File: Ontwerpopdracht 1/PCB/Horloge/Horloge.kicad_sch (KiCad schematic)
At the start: 28 parts

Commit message: update schema
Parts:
- removed S?: EVQ-P7L01P, SW_EVQ-P7L01P, symbol EVQ-P7L01P:EVQ-P7L01P
- removed Y?: FX135A-327, OSCCC150X320X90-2N, symbol FX135A-327:FX135A-327
- added U?: ATtiny412-SS, Package_SO:SOIC-8_3.9x4.9mm_P1.27mm, symbol MCU_Microchip_ATtiny:ATtiny412-SS
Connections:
- net +5V: now also S?.1_1, S?.1_1, S?.1_1, S?.1_2, S?.1_2, S?.1_2, U?.1 (VCC)
- net GND: now also U?.8 (GND)
- net +3V0: now reaches U?.3 (VIN)
- net LEDs uren: now reaches D?.4 (DIN)
- net LEDs uren: now also U?.5 (PA2)
- net Knop rechts: now reaches S?.2_1, S?.2_2
- net Knop rechts: now also U?.2 (PA6)
- net Knop midden: now reaches S?.2_1, S?.2_2
- net Knop midden: now also U?.3 (PA7)
- net Knop links: now reaches S?.2_1, S?.2_2
- net Knop links: now also U?.4 (PA1)
- net LEDs minuten: now reaches D?.4 (DIN)
- net LEDs minuten: now also U?.7 (PA3)
- new net Programming header: U?.6 (~{RESET}/PA0)
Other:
- moved on the sheet: S?, U?

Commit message: schema
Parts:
- removed D? (x20): WS2812B, LED_SMD:LED_WS2812B_PLCC4_5.0x5.0mm_P3.2mm, symbol LED:WS2812B
- removed U?: LDL1117S50R_, SOT230P700X180-4N, symbol LDL1117S50R_:LDL1117S50R_
- removed U?: ATtiny412-SS, Package_SO:SOIC-8_3.9x4.9mm_P1.27mm, symbol MCU_Microchip_ATtiny:ATtiny412-SS
- added BT1: Battery_Cell, symbol Device:Battery_Cell
- added D10, D11, D12, D13, D14, D15, D16, D17, D18, D19, D20, D21, D22, D23, D24, D3, D4, D5, D6, D7, D8, D9: WS2812B, LED_SMD:LED_WS2812B-2020_PLCC4_2.0x2.0mm, symbol LED:WS2812B
- added J1: Conn_01x03, symbol Connector_Generic:Conn_01x03
- added J1, J2: Conn_01x01, symbol Connector_Generic:Conn_01x01
- added Q1: BSS138, Package_TO_SOT_SMD:SOT-23, symbol Transistor_FET:BSS138
- added U1: TPS613222ADBVT, TPS613222ADBVT:SOT95P280X145-5N, symbol TPS613222ADBVT:TPS613222ADBVT
- added U1: ATTINY1614-SSF, ATTINY1614-SSF:SOIC127P600X175-14N, symbol ATTINY1614-SSF:ATTINY1614-SSF
- added Y1: FX135A-327, FX135A-327:OSCCC150X320X90-2N, symbol FX135A-327:FX135A-327
- D1, D2: renamed from D?; footprint LED_SMD:LED_WS2812B_PLCC4_5.0x5.0mm_P3.2mm -> LED_SMD:LED_WS2812B-2020_PLCC4_2.0x2.0mm
- S1, S2, S3: renamed from S?; footprint SW_EVQ-P7L01P -> EVQ-P7L01P:SW_EVQ-P7L01P
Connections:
- net +5V: now also J1.1 (Pin_1), Q1.2 (S), U1.1 (VDD), U1.4 (VOUT); no longer D1.3 (VSS), D2.3 (VSS)
- net GND: now also BT1.2 (-), D10.1 (VDD), D11.1 (VDD), D12.1 (VDD), D13.1 (VDD), D14.1 (VDD), D15.1 (VDD), D16.1 (VDD), D17.1 (VDD), D18.1 (VDD), D19.1 (VDD), D20.1 (VDD), D21.1 (VDD), D22.1 (VDD), D23.1 (VDD), D24.1 (VDD), D3.1 (VDD), D4.1 (VDD), D5.1 (VDD), D6.1 (VDD), D7.1 (VDD), D8.1 (VDD), D9.1 (VDD), J1.3 (Pin_3), U1.14 (GND), U1.2 (GND)
- net Knop links: now also U1.9 (PB0)
- net Knop midden: now also U1.5 (PA7)
- net Knop rechts: now also U1.4 (PA6)
- net LEDs minuten: now also D13.4 (DIN), J2.1 (Pin_1), U1.11 (PA1)
- net LEDs uren: now also J1.1 (Pin_1), U1.12 (PA2)
- net at D2.2 (DOUT): now also D3.4 (DIN)
- new net: D15.2 (DOUT), D16.4 (DIN)
- new net: D14.2 (DOUT), D15.4 (DIN)
- new net: D13.2 (DOUT), D14.4 (DIN)
- new net: D22.2 (DOUT), D23.4 (DIN)
- new net: D21.2 (DOUT), D22.4 (DIN)
- new net: D6.2 (DOUT), D7.4 (DIN)
- new net: D5.2 (DOUT), D6.4 (DIN)
- new net: D8.2 (DOUT), D9.4 (DIN)
- new net: D7.2 (DOUT), D8.4 (DIN)
- new net: D17.2 (DOUT), D18.4 (DIN)
- new net: D16.2 (DOUT), D17.4 (DIN)
- new net: D23.2 (DOUT), D24.4 (DIN)
- new net: D11.2 (DOUT), D12.4 (DIN)
- new net: D10.2 (DOUT), D11.4 (DIN)
- new net: D10.4 (DIN), D9.2 (DOUT)
- new net: D4.2 (DOUT), D5.4 (DIN)
- new net: D20.2 (DOUT), D21.4 (DIN)
- new net: D19.2 (DOUT), D20.4 (DIN)
- new net: D3.2 (DOUT), D4.4 (DIN)
- new net: D18.2 (DOUT), D19.4 (DIN)
- new net LEDs uit: Q1.1 (G), U1.8 (PB1)
- new net TOSC1: U1.6 (PB3/OSC1), Y1.1
- new net TOSC2: U1.7 (PB2/OSC2), Y1.2
- new net UDPI: J1.2 (Pin_2), U1.10 (PA0/~{RESET~{/UDPI})
- new net VCC: BT1.1 (+), U1.1 (SW)
- new net VSS: D1.3 (VSS), D10.3 (VSS), D11.3 (VSS), D12.3 (VSS), D13.3 (VSS), D14.3 (VSS), D15.3 (VSS), D16.3 (VSS), D17.3 (VSS), D18.3 (VSS), D19.3 (VSS), D2.3 (VSS), D20.3 (VSS), D21.3 (VSS), D22.3 (VSS), D23.3 (VSS), D24.3 (VSS), D3.3 (VSS), D4.3 (VSS), D5.3 (VSS), D6.3 (VSS), D7.3 (VSS), D8.3 (VSS), D9.3 (VSS), Q1.3 (D)
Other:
- note added: "ATTINY1614-SSF"
- note added: "BATTERIJ"
- note added: "KNOPPEN"
- note added: "KRISTAL"
- note added: "LED SWITCH"
- note added: "LEDS MINUTEN"
- note added: "LEDS UREN"
- note added: "PROGRAMMEERPIN"
- note added: "SPANNINGSREGELAAR"
- moved on the sheet: D1, D2, S1, S2, S3

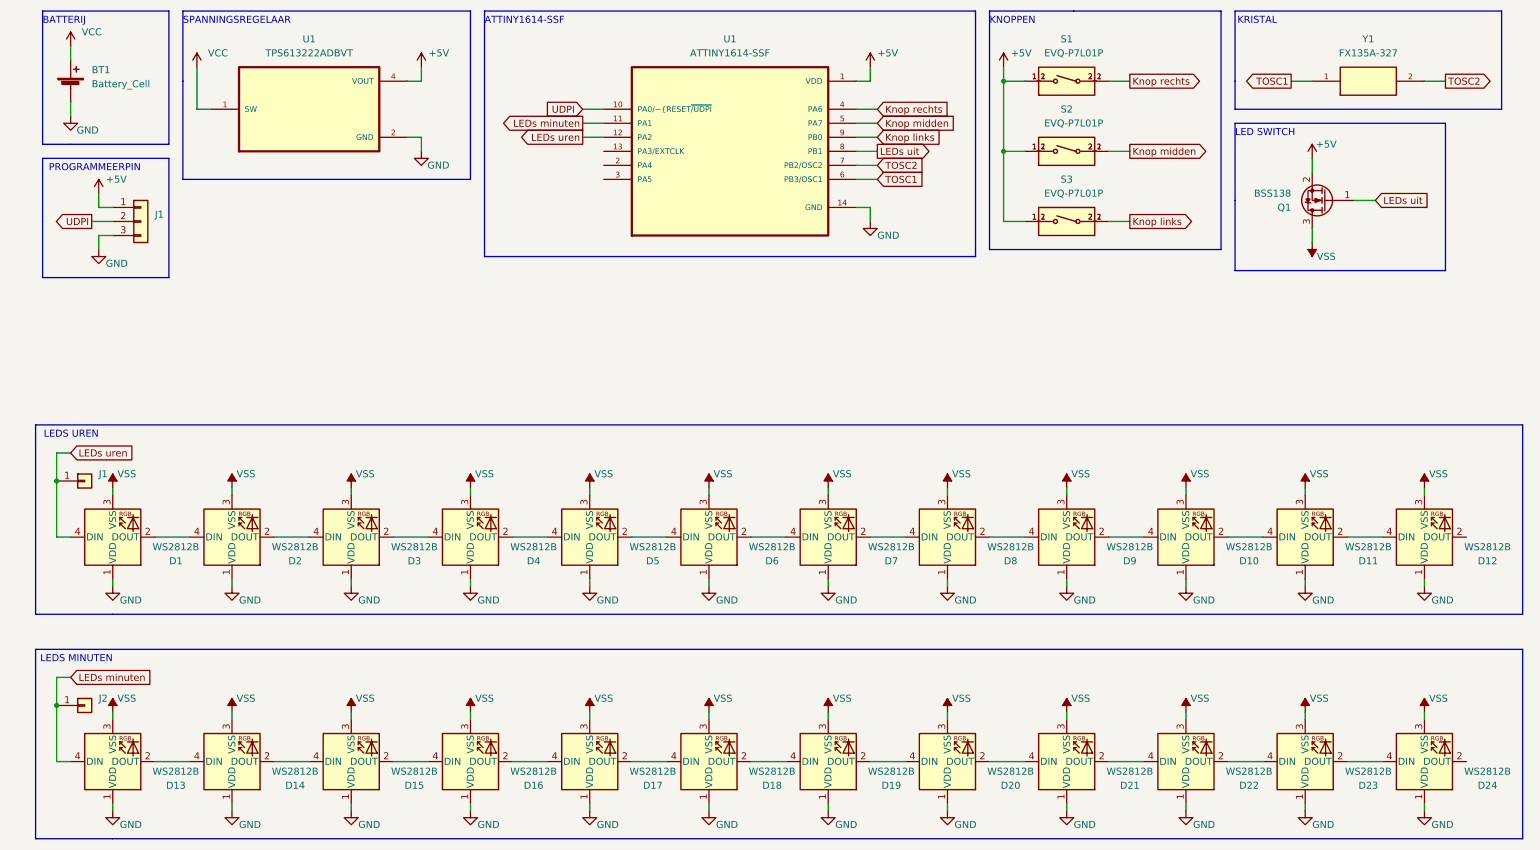
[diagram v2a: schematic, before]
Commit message: update schema + doc scema
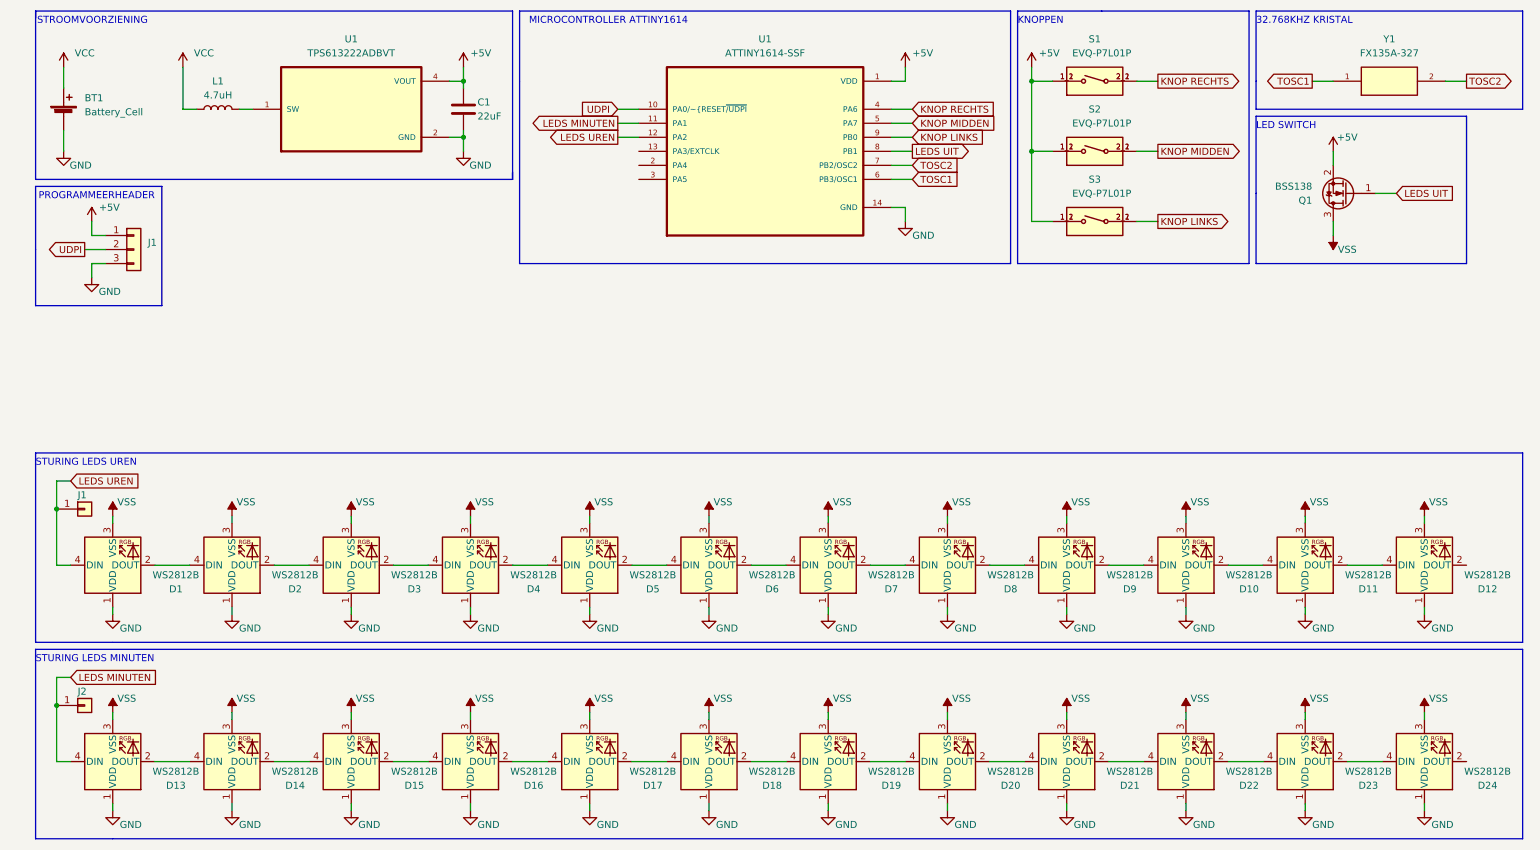
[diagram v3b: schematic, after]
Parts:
- added C1: 22uF, symbol Device:C
- added L1: 4.7uH, symbol Device:L
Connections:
- net +5V: now also C1.1
- net GND: now also C1.2
- net VCC: now also L1.1; no longer U1.1 (SW)
- net Knop links renamed KNOP LINKS
- net Knop midden renamed KNOP MIDDEN
- net Knop rechts renamed KNOP RECHTS
- net LEDs minuten renamed LEDS MINUTEN
- net LEDs uit renamed LEDS UIT
- net LEDs uren renamed LEDS UREN
- new net: L1.2, U1.1 (SW)
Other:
- note added: "32.768KHZ KRISTAL"
- note added: "MICROCONTROLLER ATTINY1614"
- note added: "PROGRAMMEERHEADER"
- note added: "STROOMVOORZIENING"
- note added: "STURING LEDS MINUTEN"
- note added: "STURING LEDS UREN"
- note removed: "ATTINY1614-SSF"
- note removed: "BATTERIJ"
- note removed: "KRISTAL"
- note removed: "LEDS MINUTEN"
- note removed: "LEDS UREN"
- note removed: "PROGRAMMEERPIN"
- note removed: "SPANNINGSREGELAAR"
- moved on the sheet: BT1, D1, D10, D11, D12, D2, D3, D4, D5, D6, D7, D8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

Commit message: aanpassing attiny, update doc schema
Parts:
- removed U1: ATTINY1614-SSF, ATTINY1614-SSF:SOIC127P600X175-14N, symbol ATTINY1614-SSF:ATTINY1614-SSF
- added U1: ATTINY414-SSF, SOIC127P600X175-14N, symbol ATTINY414-SSF:ATTINY414-SSF
- C1: footprint (none) -> GRM21BR61A226ME51L:CAPC2012X140N
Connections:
- net +5V: now also U1.1 (VDD)
- net GND: now also U1.14 (GND)
- net KNOP LINKS: now also U1.8 (PB1)
- net KNOP MIDDEN: now also U1.5 (PA7)
- net KNOP RECHTS: now also U1.4 (PA6)
- net LEDS MINUTEN: now also U1.11 (PA1)
- net LEDS UIT: now also U1.9 (PB0)
- net LEDS UREN: now also U1.12 (PA2)
- net TOSC1: now also U1.6 (TOSC1/PB3)
- net TOSC2: now also U1.7 (TOSC2/PB2)
- net UDPI: now also U1.10 (PA0/~{RESET~{/UPDI})
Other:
- note added: "MICROCONTROLLER ATTINY414"
- note removed: "MICROCONTROLLER ATTINY1614"

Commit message: aanpassing schema
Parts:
- added C2, C3: 12pF, GRM21BR61A226ME51L:CAPC2012X140N, symbol Device:C
- added R1, R2, R3: 4k7, symbol Device:R
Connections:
- net +5V: now also R1.1, R2.1, R3.1; no longer S1.1_1, S1.1_2, S2.1_1, S2.1_2, S3.1_1, S3.1_2
- net GND: now also S1.1_1, S1.1_2, S2.1_1, S2.1_2, S3.1_1, S3.1_2, C2.2, C3.2
- net KNOP LINKS: now also R3.2
- net KNOP MIDDEN: now also R2.2
- net KNOP RECHTS: now also R1.2
- net TOSC1: now also C2.1
- net TOSC2: now also C3.1
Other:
- moved on the sheet: Q1, S1, S2, S3, Y1

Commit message: update schema
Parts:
- J1: footprint (none) -> Connector_PinHeader_1.00mm:PinHeader_1x03_P1.00mm_Vertical
- J2: renamed from J1; footprint (none) -> Connector_PinHeader_2.00mm:PinHeader_1x01_P2.00mm_Vertical
- J3: renamed from J2; footprint (none) -> Connector_PinHeader_2.00mm:PinHeader_1x01_P2.00mm_Vertical
- R1, R2, R3: footprint (none) -> Resistor_SMD:R_0805_2012Metric_Pad1.20x1.40mm_HandSolder
- renumbered U1 to U2
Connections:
- net GND: now also D1.3 (VSS), D10.3 (VSS), D11.3 (VSS), D12.3 (VSS), D13.3 (VSS), D14.3 (VSS), D15.3 (VSS), D16.3 (VSS), D17.3 (VSS), D18.3 (VSS), D19.3 (VSS), D2.3 (VSS), D20.3 (VSS), D21.3 (VSS), D22.3 (VSS), D23.3 (VSS), D24.3 (VSS), D3.3 (VSS), D4.3 (VSS), D5.3 (VSS), D6.3 (VSS), D7.3 (VSS), D8.3 (VSS), D9.3 (VSS); no longer D1.1 (VDD), D10.1 (VDD), D11.1 (VDD), D12.1 (VDD), D13.1 (VDD), D14.1 (VDD), D15.1 (VDD), D16.1 (VDD), D17.1 (VDD), D18.1 (VDD), D19.1 (VDD), D2.1 (VDD), D20.1 (VDD), D21.1 (VDD), D22.1 (VDD), D23.1 (VDD), D24.1 (VDD), D3.1 (VDD), D4.1 (VDD), D5.1 (VDD), D6.1 (VDD), D7.1 (VDD), D8.1 (VDD), D9.1 (VDD)
- net VSS: now also D1.1 (VDD), D10.1 (VDD), D11.1 (VDD), D12.1 (VDD), D13.1 (VDD), D14.1 (VDD), D15.1 (VDD), D16.1 (VDD), D17.1 (VDD), D18.1 (VDD), D19.1 (VDD), D2.1 (VDD), D20.1 (VDD), D21.1 (VDD), D22.1 (VDD), D23.1 (VDD), D24.1 (VDD), D3.1 (VDD), D4.1 (VDD), D5.1 (VDD), D6.1 (VDD), D7.1 (VDD), D8.1 (VDD), D9.1 (VDD); no longer D1.3 (VSS), D10.3 (VSS), D11.3 (VSS), D12.3 (VSS), D13.3 (VSS), D14.3 (VSS), D15.3 (VSS), D16.3 (VSS), D17.3 (VSS), D18.3 (VSS), D19.3 (VSS), D2.3 (VSS), D20.3 (VSS), D21.3 (VSS), D22.3 (VSS), D23.3 (VSS), D24.3 (VSS), D3.3 (VSS), D4.3 (VSS), D5.3 (VSS), D6.3 (VSS), D7.3 (VSS), D8.3 (VSS), D9.3 (VSS)

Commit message: pcb
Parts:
- C1, C2, C3: footprint GRM21BR61A226ME51L:CAPC2012X140N -> Capacitor_SMD:C_0805_2012Metric_Pad1.18x1.45mm_HandSolder
- L1: footprint (none) -> Inductor_SMD:L_Sunlord_SWPA5020S
- U2: footprint SOIC127P600X175-14N -> ATTINY414-SSF:SOIC127P600X175-14N
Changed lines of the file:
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@@
       (effects (font (size 1.27 1.27)) (justify left))
     )
-    (property "Footprint" "GRM21BR61A226ME51L:CAPC2012X140N" (id 2) (at 51.7652 68.58 0)
+    (property "Footprint" "Capacitor_SMD:C_0805_2012Metric_Pad1.18x1.45mm_HandSolder" (id 2) (at 51.7652 68.58 0)
       (effects (font (size 1.27 1.27)) hide)
     )
@@
     (property "Reference" "U2" (id 0) (at 146.05 19.05 0))
     (property "Value" "ATTINY414-SSF" (id 1) (at 146.05 21.59 0))
-    (property "Footprint" "SOIC127P600X175-14N" (id 2) (at 146.05 39.37 0)
+    (property "Footprint" "ATTINY414-SSF:SOIC127P600X175-14N" (id 2) (at 146.05 39.37 0)
       (effects (font (size 1.27 1.27)) (justify bottom) hide)
     )
@@
       (effects (font (size 1.27 1.27)) (justify left))
     )
-    (property "Footprint" "GRM21BR61A226ME51L:CAPC2012X140N" (id 2) (at 92.4052 35.56 0)
+    (property "Footprint" "Capacitor_SMD:C_0805_2012Metric_Pad1.18x1.45mm_HandSolder" (id 2) (at 92.4052 35.56 0)
       (effects (font (size 1.27 1.27)) hide)
     )
@@
     (property "Reference" "L1" (id 0) (at 46.99 26.67 90))
     (property "Value" "4.7uH" (id 1) (at 46.99 29.21 90))
-    (property "Footprint" "" (id 2) (at 46.99 31.75 0)
+    (property "Footprint" "Inductor_SMD:L_Sunlord_SWPA5020S" (id 2) (at 46.99 31.75 0)
       (effects (font (size 1.27 1.27)) hide)
     )
@@
       (effects (font (size 1.27 1.27)) (justify left))
     )
-    (property "Footprint" "GRM21BR61A226ME51L:CAPC2012X140N" (id 2) (at 77.1652 68.58 0)
+    (property "Footprint" "Capacitor_SMD:C_0805_2012Metric_Pad1.18x1.45mm_HandSolder" (id 2) (at 77.1652 68.58 0)
       (effects (font (size 1.27 1.27)) hide)
     )
@@
     )
     (path "/d7e56d45-a657-43fb-bc8b-670c5cd57934"
-      (reference "C1") (unit 1) (value "22uF") (footprint "GRM21BR61A226ME51L:CAPC2012X140N")
+      (reference "C1") (unit 1) (value "22uF") (footprint "Capacitor_SMD:C_0805_2012Metric_Pad1.18x1.45mm_HandSolder")
     )
     (path "/0cda8030-1957-40fa-9ada-a2819489c5e2"
-      (reference "C2") (unit 1) (value "12pF") (footprint "GRM21BR61A226ME51L:CAPC2012X140N")
+      (reference "C2") (unit 1) (value "12pF") (footprint "Capacitor_SMD:C_0805_2012Metric_Pad1.18x1.45mm_HandSolder")
     )
     (path "/f9b52ee3-acc0-4d75-9513-ba7c704b696b"
-      (reference "C3") (unit 1) (value "12pF") (footprint "GRM21BR61A226ME51L:CAPC2012X140N")
+      (reference "C3") (unit 1) (value "12pF") (footprint "Capacitor_SMD:C_0805_2012Metric_Pad1.18x1.45mm_HandSolder")
     )
     (path "/24e64655-404c-4e7d-966c-1f2b57c66a95"
@@
     )
     (path "/e8b02372-df70-4a53-bb2e-192ce2085ac9"
-      (reference "L1") (unit 1) (value "4.7uH") (footprint "")
+      (reference "L1") (unit 1) (value "4.7uH") (footprint "Inductor_SMD:L_Sunlord_SWPA5020S")
     )
     (path "/a028ea2d-9fb9-4ae1-816d-39a67e196c9a"
@@
     )
     (path "/987d473b-352b-41d0-80e0-69799be27f92"
-      (reference "U2") (unit 1) (value "ATTINY414-SSF") (footprint "SOIC127P600X175-14N")
+      (reference "U2") (unit 1) (value "ATTINY414-SSF") (footprint "ATTINY414-SSF:SOIC127P600X175-14N")
     )
     (path "/dd963ad9-8348-4889-b2f7-109bf8f9c02d"
